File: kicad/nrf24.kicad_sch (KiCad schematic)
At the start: 19 parts, among them J1 Conn_Coaxial, U1 nRF24L01P, X2 16MHz

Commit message: readme and journal
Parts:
- removed X2: 16MHz, Crystal:Crystal_HC52-U_Vertical, symbol Crystal_AKL:Crystal_Generic
- added X1: 16MHz, Crystal:Crystal_HC52-U_Vertical, symbol Crystal_AKL:Crystal_Generic
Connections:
- net XTAL_N: now reaches C6.1, R2.1
- net XTAL_N: now also U1.10 (XC1), X1.1; no longer U1.9 (XC2)
- net XTAL_P: now reaches C9.1, R2.2
- net XTAL_P: now also U1.9 (XC2), X1.2; no longer U1.10 (XC1)
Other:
- note added: "rfx2401c?"
- note added: "what does this do? i have no idea"
- moved on the sheet: C10, C11, C7, C8, J1, L2, L3

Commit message: journal and image
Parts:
- removed C10: 15pF, Capacitor_SMD:C_0603_1608Metric, symbol Device:C_Small
- removed C11: 1.5pF, Capacitor_SMD:C_0603_1608Metric, symbol Device:C_Small
- removed J1: Conn_Coaxial, Connector_Coaxial:SMA_Amphenol_901-143_Horizontal, symbol Connector:Conn_Coaxial
- removed L3: 7.9nH, Inductor_SMD:L_0603_1608Metric, symbol Device:L_Small
- renumbered C7 to C6, C8 to C7, C6 to C8, L2 to L1, L1 to L2
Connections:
- net ANT: now reaches L2.2, U1.13 (ANT2)
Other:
- note added: "power hungry indeed"
- note added: "to mcu"

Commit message: add rfx2401c
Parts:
- added C8: 15pF, Capacitor_SMD:C_0603_1608Metric, symbol Device:C_Small
- added C9: 1.5pF, Capacitor_SMD:C_0603_1608Metric, symbol Device:C_Small
- added L3: 7.9nH, Inductor_SMD:L_0603_1608Metric, symbol Device:L_Small
- renumbered C8 to C10, C9 to C11
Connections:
- net ANT: now also C8.2, C9.2; no longer L2.2, U1.13 (ANT2)
- net GND: now also C9.1
- net VDD_PA: now reaches C6.2, C7.2, L1.1, U1.11 (VDD_PA)
- net VCC renamed +3.3V
- new net: L2.2, L3.1, U1.13 (ANT2)
- new net: C8.1, L3.2
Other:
- note removed: "rfx2401c?"

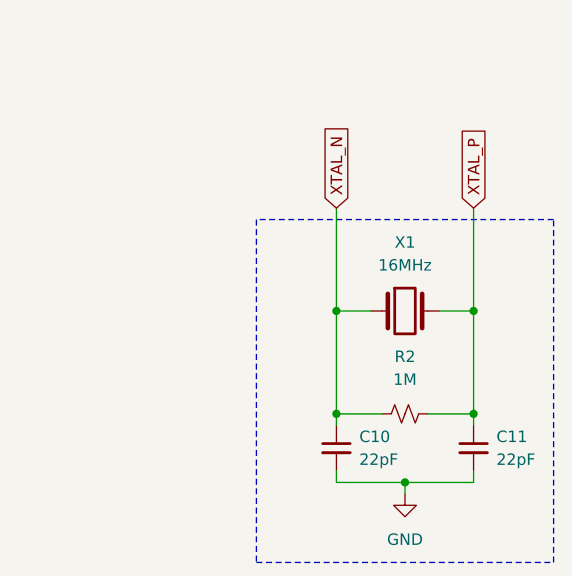
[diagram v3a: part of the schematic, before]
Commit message: change crystal footprint
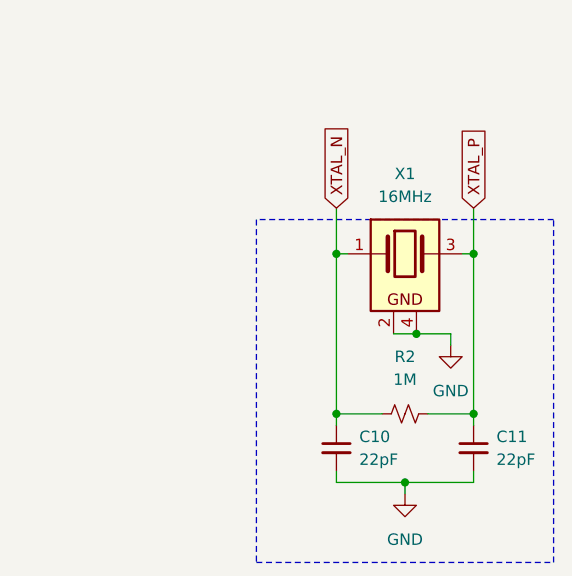
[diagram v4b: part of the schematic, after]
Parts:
- removed X1: 16MHz, Crystal:Crystal_HC52-U_Vertical, symbol Crystal_AKL:Crystal_Generic
- added X1: 16MHz, Crystal:Crystal_SMD_3225-4Pin_3.2x2.5mm, symbol Crystal_AKL:Crystal_Generic_GND24
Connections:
- net GND: now also X1.2, X1.4
- net XTAL_N: now also X1.1
- net XTAL_P: now also X1.3
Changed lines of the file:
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@@
+	)
+	(junction
+		(at 154.94 146.05)
+		(diameter 0)
+		(color 0 0 0 0)
+	)
+	(junction
+		(at 139.7 146.05)
+		(diameter 0)
+		(color 0 0 0 0)
 	)
 	(junction
@@
 	)
 	(junction
+		(at 148.59 154.94)
+		(diameter 0)
+		(color 0 0 0 0)
+	)
+	(junction
 		(at 80.01 31.75)
 		(diameter 0)
@@
 	)
 	(junction
-		(at 154.94 152.4)
-		(diameter 0)
-		(color 0 0 0 0)
-	)
-	(junction
 		(at 154.94 163.83)
 		(diameter 0)
@@
 	)
 	(junction
-		(at 139.7 152.4)
-		(diameter 0)
-		(color 0 0 0 0)
-	)
-	(junction
 		(at 92.71 86.36)
 		(diameter 0)
@@
 	(wire
 		(pts
+			(xy 146.05 154.94) (xy 148.59 154.94)
+		)
+		(stroke
+			(width 0)
+			(type default)
+		)
+	)
+	(wire
+		(pts
 			(xy 80.01 31.75) (xy 92.71 31.75)
 		)
@@
 	(wire
 		(pts
-			(xy 139.7 140.97) (xy 139.7 152.4)
+			(xy 139.7 140.97) (xy 139.7 146.05)
 		)
 		(stroke
@@
 	(wire
 		(pts
+			(xy 152.4 156.21) (xy 152.4 154.94)
+		)
+		(stroke
+			(width 0)
+			(type default)
+		)
+	)
+	(wire
+		(pts
 			(xy 77.47 77.47) (xy 71.12 77.47)
 		)
@@
 	(wire
 		(pts
-			(xy 154.94 140.97) (xy 154.94 152.4)
+			(xy 154.94 140.97) (xy 154.94 146.05)
 		)
 		(stroke
@@
 		)
 	)
+	(wire
+		(pts
+			(xy 148.59 154.94) (xy 152.4 154.94)
+		)
+		(stroke
+			(width 0)
+			(type default)
+		)
+	)
 	(polyline
 		(pts
@@
 	(wire
 		(pts
-			(xy 154.94 152.4) (xy 154.94 163.83)
-		)
-		(stroke
-			(width 0)
-			(type default)
-		)
-	)
-	(wire
-		(pts
 			(xy 139.7 171.45) (xy 147.32 171.45)
 		)
@@
 	(wire
 		(pts
-			(xy 151.13 152.4) (xy 154.94 152.4)
-		)
-		(stroke
-			(width 0)
-			(type default)
-		)
-	)
-	(wire
-		(pts
-			(xy 139.7 152.4) (xy 143.51 152.4)
+			(xy 139.7 146.05) (xy 140.97 146.05)
 		)
 		(stroke
@@
 	(wire
 		(pts
+			(xy 139.7 146.05) (xy 139.7 163.83)
+		)
+		(stroke
+			(width 0)
+			(type default)
+		)
+	)
+	(wire
+		(pts
 			(xy 76.2 52.07) (xy 77.47 52.07)
 		)
@@
 	(wire
 		(pts
-			(xy 139.7 152.4) (xy 139.7 163.83)
-		)
-		(stroke
-			(width 0)
-			(type default)
-		)
-	)
-	(wire
-		(pts
 			(xy 76.2 59.69) (xy 77.47 59.69)
 		)
@@
 	(wire
 		(pts
+			(xy 153.67 146.05) (xy 154.94 146.05)
+		)
+		(stroke
+			(width 0)
+			(type default)
+		)
+	)
+	(wire
+		(pts
 			(xy 97.79 85.09) (xy 97.79 86.36)
 		)
@@
 		(pts
 			(xy 107.95 62.23) (xy 109.22 62.23)
+		)
+		(stroke
+			(width 0)
+			(type default)
+		)
+	)
+	(wire
+		(pts
+			(xy 154.94 146.05) (xy 154.94 163.83)
 		)
 		(stroke
@@
 			)
 			(justify right)
+		)
+	)
+	(symbol
+		(lib_name "GND_1")
+		(lib_id "power:GND")
+		(at 152.4 156.21 0)
+		(unit 1)
+		(body_style 1)
+		(exclude_from_sim no)
+		(in_bom yes)
+		(on_board yes)
+		(in_pos_files yes)
+		(dnp no)
+		(fields_autoplaced yes)
+		(property "Reference" "#PWR07"
+			(at 152.4 162.56 0)
+			(hide yes)
+			(show_name no)
+			(do_not_autoplace no)
+			(effects
+				(font
+					(size 1.27 1.27)
+				)
+			)
+		)
+		(property "Value" "GND"
+			(at 152.4 161.29 0)
+			(show_name no)
+			(do_not_autoplace no)
+			(effects
+				(font
+					(size 1.27 1.27)
+				)
+			)
+		)
+		(property "Footprint" ""
+			(at 152.4 156.21 0)
+			(hide yes)
+			(show_name no)
+			(do_not_autoplace no)
+			(effects
+				(font
+					(size 1.27 1.27)
+				)
+			)
+		)
+		(property "Datasheet" ""
+			(at 152.4 156.21 0)
+			(hide yes)
+			(show_name no)
+			(do_not_autoplace no)
+			(effects
+				(font
+					(size 1.27 1.27)
+				)
+			)
+		)
+		(property "Description" ""
+			(at 152.4 156.21 0)
+			(hide yes)
+			(show_name no)
+			(do_not_autoplace no)
+			(effects
+				(font
+					(size 1.27 1.27)
+				)
+			)
+		)
+		(pin "1"
+		)
+		(instances
+			(project "nRF24"
+				(path "/27c3244d-bba8-40dc-af7b-5db1a6f17f49/02669cf5-de35-4512-b002-009131b5189c"
+					(reference "#PWR07")
+					(unit 1)
+				)
+			)
 		)
 	)
@@
 	)
 	(symbol
+		(lib_id "Crystal_AKL:Crystal_Generic_GND24")
+		(at 147.32 146.05 0)
+		(unit 1)
+		(body_style 1)
+		(exclude_from_sim no)
+		(in_bom yes)
+		(on_board yes)
+		(in_pos_files yes)
+		(dnp no)
+		(fields_autoplaced yes)
+		(property "Reference" "X1"
+			(at 147.32 137.16 0)
+			(show_name no)
+			(do_not_autoplace no)
+			(effects
+				(font
+					(size 1.27 1.27)
+				)
+			)
+		)
+		(property "Value" "16MHz"
+			(at 147.32 139.7 0)
+			(show_name no)
+			(do_not_autoplace no)
+			(effects
+				(font
+					(size 1.27 1.27)
+				)
+			)
+		)
+		(property "Footprint" "Crystal:Crystal_SMD_3225-4Pin_3.2x2.5mm"
+			(at 147.32 146.05 0)
+			(hide yes)
+			(show_name no)
+			(do_not_autoplace no)
+			(effects
+				(font
+					(size 1.27 1.27)
+				)
+			)
+		)
+		(property "Datasheet" ""
+			(at 147.32 146.05 0)
+			(hide yes)
+			(show_name no)
+			(do_not_autoplace no)
+			(effects
+				(font
+					(size 1.27 1.27)
+				)
+			)
+		)
+		(property "Description" "Quartz crystal, Shielded, Generic symbol, Alternate KiCad Library"
+			(at 147.32 146.05 0)
+			(hide yes)
+			(show_name no)
+			(do_not_autoplace no)
+			(effects
+				(font
+					(size 1.27 1.27)
+				)
+			)
+		)
+		(pin "2"
+		)
+		(pin "1"
+		)
+		(pin "3"
+		)
+		(pin "4"
+		)
+		(instances
+			(project "nRF24"
+				(path "/27c3244d-bba8-40dc-af7b-5db1a6f17f49/02669cf5-de35-4512-b002-009131b5189c"
+					(reference "X1")
+					(unit 1)
+				)
+			)
+		)
+	)
+	(symbol
 		(lib_id "power:GND")
 		(at 93.98 87.63 0)
@@
 					(unit 1)
 				)
-			)
-		)
-	)
-	(symbol
-		(lib_id "Crystal_AKL:Crystal_Generic")
-		(at 147.32 152.4 0)
-		(unit 1)
-		(body_style 1)
-		(exclude_from_sim no)
-		(in_bom yes)
-		(on_board yes)
-		(in_pos_files yes)
-		(dnp no)
-		(fields_autoplaced yes)
-		(property "Reference" "X1"
-			(at 147.32 144.78 0)
-			(show_name no)
-			(do_not_autoplace no)
-			(effects
-				(font
-					(size 1.27 1.27)
-				)
-			)
-		)
-		(property "Value" "16MHz"
-			(at 147.32 147.32 0)
-			(show_name no)
-			(do_not_autoplace no)
-			(effects
-				(font
-					(size 1.27 1.27)
-				)
-			)
-		)
-		(property "Footprint" "Crystal:Crystal_HC52-U_Vertical"
-			(at 147.32 152.4 0)
-			(hide yes)
-			(show_name no)
-			(do_not_autoplace no)
-			(effects
-				(font
-					(size 1.27 1.27)
-				)
-			)
-		)
-		(property "Datasheet" ""
-			(at 147.32 152.4 0)
-			(hide yes)
-			(show_name no)
-			(do_not_autoplace no)
-			(effects
-				(font
-					(size 1.27 1.27)
-				)
-			)
-		)
-		(property "Description" "Quartz crystal, Generic symbol, Alternate KiCad Library"
-			(at 147.32 152.4 0)
-			(hide yes)
-			(show_name no)
-			(do_not_autoplace no)
-			(effects
-				(font
-					(size 1.27 1.27)
-				)
-			)
-		)
-		(pin "2"
-		)
-		(pin "1"
-		)
-		(instances
-			(project "nRF24"
-				(path "/27c3244d-bba8-40dc-af7b-5db1a6f17f49/02669cf5-de35-4512-b002-009131b5189c"
-					(reference "X1")
-					(unit 1)
-				)

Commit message: journal images and reamde
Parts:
- L1, L3: footprint Inductor_SMD:L_0603_1608Metric -> Inductor_SMD:L_0402_1005Metric
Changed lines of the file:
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@@
 			)
 		)
-		(property "Footprint" "Inductor_SMD:L_0603_1608Metric"
+		(property "Footprint" "Inductor_SMD:L_0402_1005Metric"
 			(at 109.22 54.61 0)
 			(hide yes)
@@
 			)
 		)
-		(property "Footprint" "Inductor_SMD:L_0603_1608Metric"
+		(property "Footprint" "Inductor_SMD:L_0402_1005Metric"
 			(at 123.19 62.23 0)
 			(hide yes)
